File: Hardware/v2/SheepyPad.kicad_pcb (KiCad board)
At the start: 2 copper layers, 127.6 x 99.7 mm, 60 parts, among them SW1 SW_Push, SW2 Rotary_Encoder_Switch, U1 Sparkfun_Pro_Micro

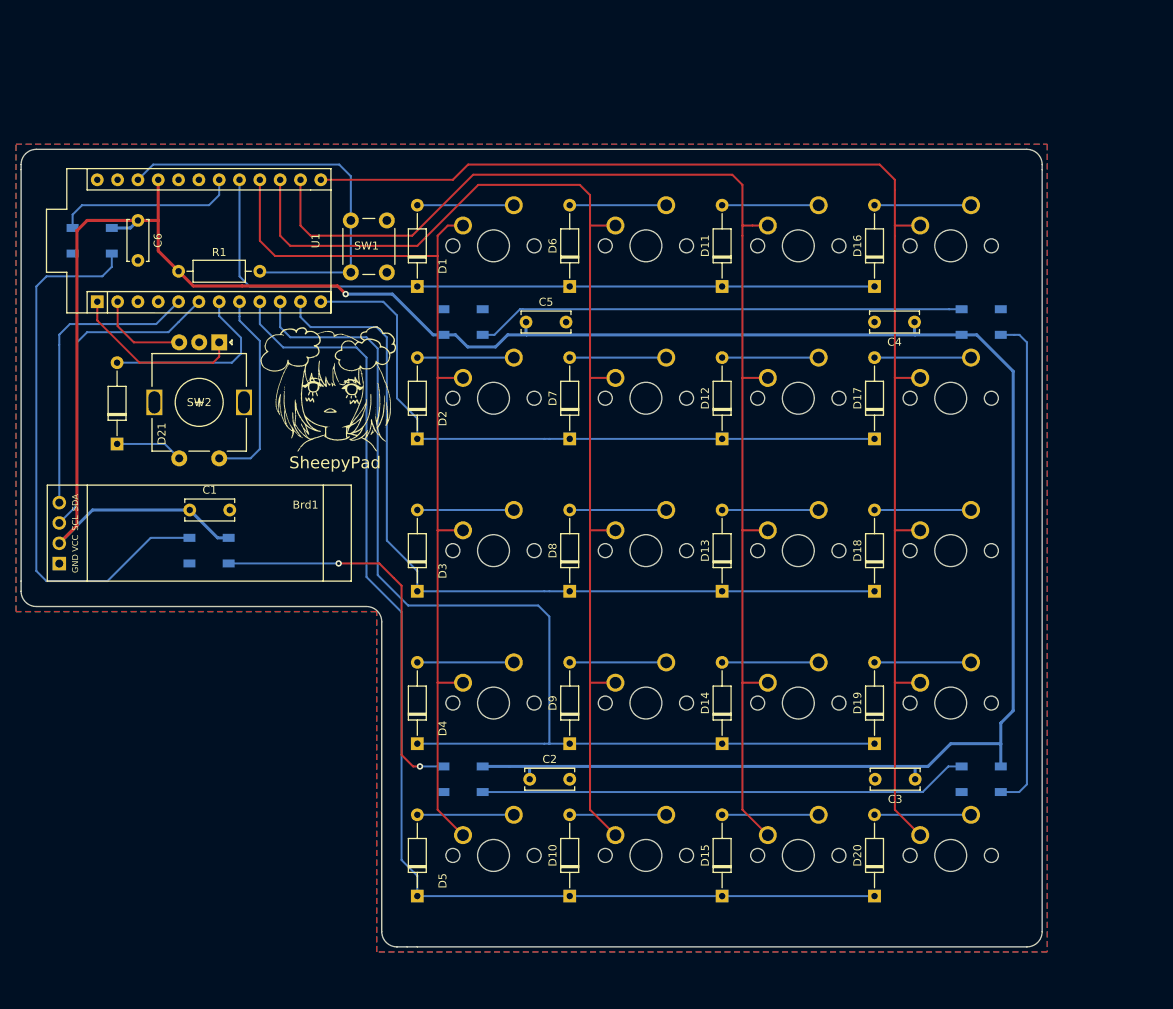
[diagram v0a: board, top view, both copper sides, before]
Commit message: Remove of redundant lib
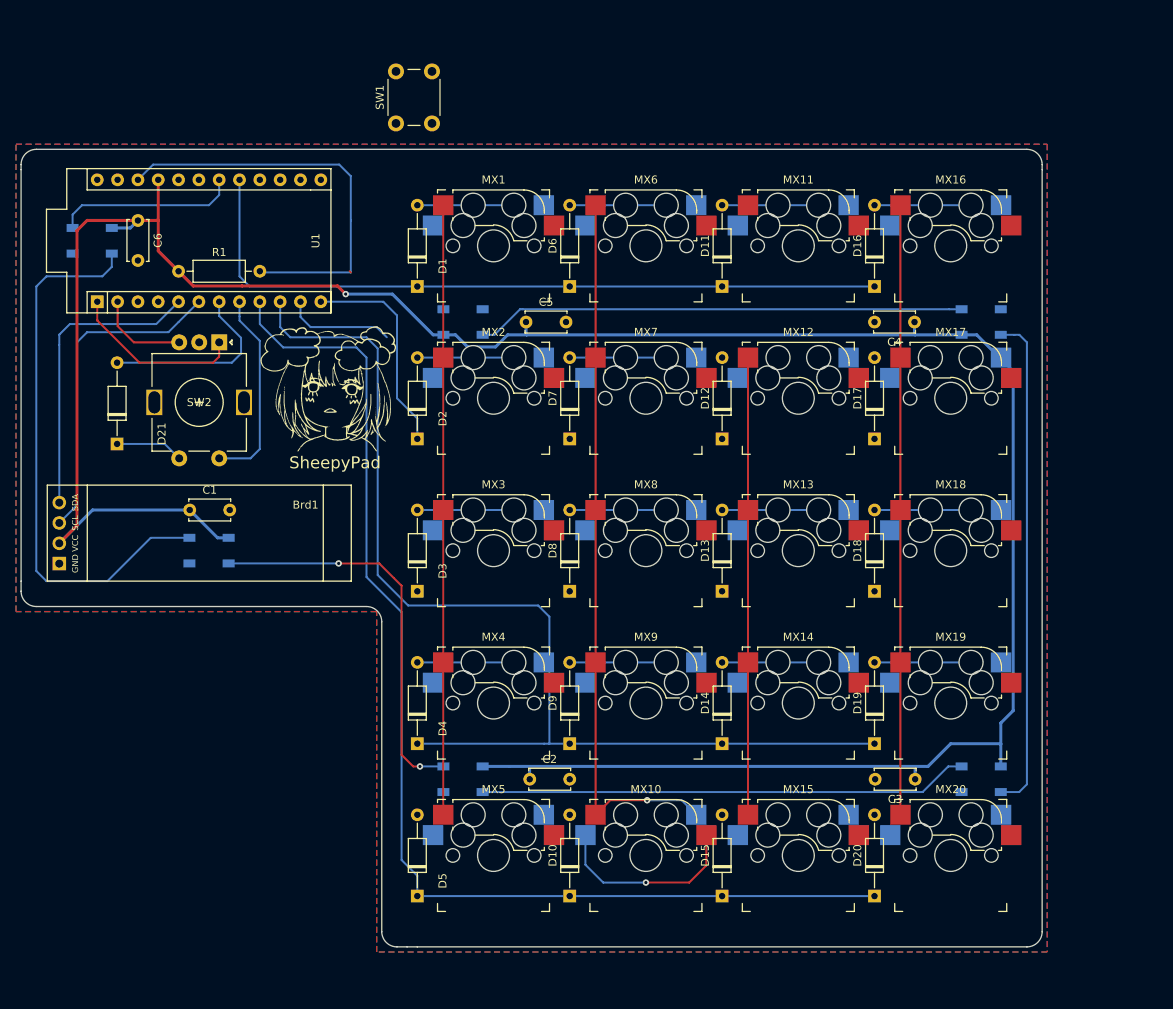
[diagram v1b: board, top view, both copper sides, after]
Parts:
- C1, C2, C3, C4, C5: footprint Capacitor_THT:C_Disc_D6.0mm_W2.5mm_P5.00mm -> Capacitor_THT:C_Disc_D5.0mm_W2.5mm_P5.00mm
- MX1, MX10, MX11, MX12, MX13, MX14, MX15, MX16, MX17, MX18, MX19, MX2, MX20, MX3, MX4, MX5, MX6, MX7, MX8, MX9: footprint MX_Only:MXOnly-1U-NoLED -> Keyswitches:Kailh_socket_MX_optional_reversible_FLIP
- moved SW1 12.2 mm to (104.0, 39.9), turned to 90 degrees
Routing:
- net /COL_3: track 160.5 -> 57.1 mm
- net /COL_4: track 169.3 -> 76.2 mm
- net /ROW_3: track 104.2 -> 13.8 mm
- net /ROW_2: track 83.9 -> 26.7 mm
- net /COL_2: track 144.0 -> 90.3 mm, vias 0 -> 1
- net /COL_1: track 120.1 -> 76.2 mm
- net Net-(D10-Pad2): track 12.1 -> 26.2 mm, vias 0 -> 1
- net Net-(D5-Pad2): track 12.1 -> 0.00 mm
- net Net-(D20-Pad2): track 12.1 -> 0.00 mm
- net Net-(D17-Pad2): track 12.1 -> 0.00 mm
- net Net-(D15-Pad2): track 12.1 -> 0.00 mm
- net Net-(D12-Pad2): track 12.1 -> 0.00 mm

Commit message: WIP v2
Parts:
- added D22: WS2812B, LED_SMD:LED_WS2812B_PLCC4_5.0x5.0mm_P3.2mm, F.Cu at (66.0, 54.6)
- added D23: WS2812B, LED_SMD:LED_WS2812B_PLCC4_5.0x5.0mm_P3.2mm, F.Cu at (180.3, 120.7)
- added D24: WS2812B, LED_SMD:LED_WS2812B_PLCC4_5.0x5.0mm_P3.2mm, F.Cu at (80.6, 93.3)
- added D25: WS2812B, LED_SMD:LED_WS2812B_PLCC4_5.0x5.0mm_P3.2mm, F.Cu at (180.3, 63.4)
- added D26: WS2812B, LED_SMD:LED_WS2812B_PLCC4_5.0x5.0mm_P3.2mm, F.Cu at (109.3, 120.7)
- added D27: WS2812B, LED_SMD:LED_WS2812B_PLCC4_5.0x5.0mm_P3.2mm, F.Cu at (109.3, 63.4)
- D1, D10, D11, D12, D13, D14, D15, D16, D17, D18, D19, D2, D20, D21, D3, D4, D5, D6, D7, D8, D9: footprint Diode_THT:D_DO-35_SOD27_P10.16mm_Horizontal -> Random-keyboard-parts:Diode_SMD_THT_DUAL
- moved C2 32.2 mm to (100.8, 147.3)
- moved C5 26.3 mm to (115.1, 38.9)
- moved C4 24.0 mm to (192.8, 62.7)
- moved C3 23.7 mm to (192.6, 122.3)
- moved D11 9.54 mm to (154.3, 59.8), turned to 270 degrees
- moved D12 9.54 mm to (154.3, 78.9), turned to 270 degrees
- moved D15 9.54 mm to (154.3, 136.0), turned to 270 degrees
- moved D13 9.54 mm to (154.3, 97.9), turned to 270 degrees
- moved D14 9.54 mm to (154.3, 117.0), turned to 270 degrees
- moved D1 9.54 mm to (116.2, 59.8), turned to 270 degrees
- moved D10 9.54 mm to (135.3, 136.0), turned to 270 degrees
- moved D2 9.54 mm to (116.2, 78.9), turned to 270 degrees
- moved D5 9.54 mm to (116.2, 136.0), turned to 270 degrees
- moved D6 9.54 mm to (135.3, 59.8), turned to 270 degrees
- moved D7 9.54 mm to (135.3, 78.9), turned to 270 degrees
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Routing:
- net +5V: track 324.3 -> 119.1 mm
- net /COL_3: track 57.1 -> 147.8 mm, vias 0 -> 5
- net /ROW_3: track 13.8 -> 100.3 mm
- net /COL_4: track 76.2 -> 147.8 mm, vias 0 -> 5
- net /COL_1: track 76.2 -> 147.8 mm, vias 0 -> 5
- net /ROW_2: track 26.7 -> 94.4 mm
- net Net-(D23-Pad2): track 62.6 -> 0.00 mm
- net Net-(D25-Pad2): track 61.2 -> 0.00 mm
- net Net-(D23-Pad4): track 61.2 -> 0.00 mm
- net /COL_2: track 90.3 -> 147.8 mm, vias 1 -> 5
- net Net-(D17-Pad2): track 0.00 -> 33.5 mm, vias 0 -> 1
- net Net-(D20-Pad2): track 0.00 -> 33.5 mm, vias 0 -> 1
- net Net-(D5-Pad2): track 0.00 -> 33.5 mm, vias 0 -> 1
- net Net-(D15-Pad2): track 0.00 -> 33.5 mm, vias 0 -> 1
- net Net-(D12-Pad2): track 0.00 -> 32.7 mm, vias 0 -> 1
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
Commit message: Update v2
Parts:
- removed the G*** at (93.3, 76.8)
- removed R1: 10K, Resistor_THT:R_Axial_DIN0207_L6.3mm_D2.5mm_P10.16mm_Horizontal
- added G***: LOGO, Logos:IronMan_small, B.Cu at (68.6, 96.2)
- added G***: LOGO, Logos:IronMan_small, F.Cu at (68.6, 96.2)
- added G***: LOGO, Logos:Sleepy, B.Cu at (97.1, 72.3)
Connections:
- D1 pad 1: /ROW_1 -> /ROW_0
- D10 pad 1: /ROW_5 -> /ROW_4
- D11 pad 1: /ROW_1 -> /ROW_0
- D12 pad 1: /ROW_2 -> /ROW_1
- D13 pad 1: /ROW_3 -> /ROW_2
- D14 pad 1: /ROW_4 -> /ROW_3
- D15 pad 1: /ROW_5 -> /ROW_4
- D16 pad 1: /ROW_1 -> /ROW_0
- D17 pad 1: /ROW_2 -> /ROW_1
- D18 pad 1: /ROW_3 -> /ROW_2
- D19 pad 1: /ROW_4 -> /ROW_3
- D2 pad 1: /ROW_2 -> /ROW_1
- D20 pad 1: /ROW_5 -> /ROW_4
- D21 pad 2: /COL_ENC_1 -> /COL_0
- D22 pad 1: (no net) -> +5V
- D22 pad 2: (no net) -> Net-(D22-Pad2)
- D22 pad 3: (no net) -> GND
- D22 pad 4: (no net) -> /GLOW_LED
- D23 pad 1: (no net) -> +5V
- D23 pad 2: (no net) -> Net-(D23-Pad2)
- D23 pad 3: (no net) -> GND
- D23 pad 4: (no net) -> Net-(D23-Pad4)
- D24 pad 1: (no net) -> +5V
- D24 pad 2: (no net) -> Net-(D24-Pad2)
- D24 pad 3: (no net) -> GND
- D24 pad 4: (no net) -> Net-(D22-Pad2)
- D25 pad 1: (no net) -> +5V
- D25 pad 2: (no net) -> Net-(D25-Pad2)
- D25 pad 3: (no net) -> GND
- D25 pad 4: (no net) -> Net-(D23-Pad2)
- D26 pad 1: (no net) -> +5V
- D26 pad 2: (no net) -> Net-(D23-Pad4)
- D26 pad 3: (no net) -> GND
- D26 pad 4: (no net) -> Net-(D24-Pad2)
- D27 pad 1: (no net) -> +5V
- D27 pad 2: (no net) -> Net-(D27-Pad2)
- D27 pad 3: (no net) -> GND
- D27 pad 4: (no net) -> Net-(D25-Pad2)
- D3 pad 1: /ROW_3 -> /ROW_2
- D4 pad 1: /ROW_4 -> /ROW_3
- D5 pad 1: /ROW_5 -> /ROW_4
- D6 pad 1: /ROW_1 -> /ROW_0
- D7 pad 1: /ROW_2 -> /ROW_1
- D8 pad 1: /ROW_3 -> /ROW_2
- D9 pad 1: /ROW_4 -> /ROW_3
- SW2 pad S2: /ROW_ENC_1 -> /ROW_0
- U1 pad 1: /ENC_A -> Net-(U1-Pad1)
- U1 pad 10: /ROW_4 -> /ROW_2
- U1 pad 11: /ROW_3 -> /ROW_1
- U1 pad 12: /ROW_2 -> /ROW_0
- U1 pad 13: /COL_4 -> /COL_0
- U1 pad 14: /COL_3 -> /COL_1
- U1 pad 16: /COL_1 -> /COL_3
- U1 pad 17: /ROW_1 -> /COL_4
- U1 pad 18: /GLOW_LED -> Net-(U1-Pad18)
- U1 pad 19: Net-(U1-Pad19) -> /ENC_A
- U1 pad 2: /ENC_B -> /DATA
- U1 pad 20: Net-(U1-Pad20) -> /ENC_B
- U1 pad 7: /COL_ENC_1 -> /GLOW_LED
- U1 pad 8: /ROW_ENC_1 -> /ROW_4
- U1 pad 9: /ROW_5 -> /ROW_3
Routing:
- net /ROW_5: track 129.6 -> 0.00 mm
- net +5V: track 119.1 -> 24.5 mm, vias 1 -> 0
- net /ROW_0: track 0.00 -> 85.6 mm
- net /RESET: track 51.7 -> 0.00 mm
- net Net-(D22-Pad2): track 69.6 -> 21.9 mm
- net /ROW_4: track 129.0 -> 84.3 mm
- net /SCL: track 40.8 -> 3.13 mm
- net /SDA: track 37.6 -> 0.00 mm
- net /ROW_ENC_1: track 25.0 -> 0.00 mm
- net /COL_ENC_1: track 23.5 -> 0.00 mm
- net /GLOW_LED: track 22.9 -> 0.00 mm
- net /ENC_A: track 22.5 -> 0.64 mm
- net Net-(D24-Pad2): track 21.4 -> 0.00 mm, vias 1 -> 0
- net /ROW_3: track 100.3 -> 84.2 mm
- net /ROW_1: track 99.5 -> 86.6 mm
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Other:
- board text added: "SheepyPad v2"
- board text removed: "SheepyPad"

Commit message: WIP
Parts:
- added REF**: PJ-3200B-4A, Random-keyboard-parts:PJ-3200B-4A, B.Cu at (98.9, 43.3)
- added REF**: PJ-3200B-4A, Random-keyboard-parts:PJ-3200B-4A, F.Cu at (101.2, 43.3)
- U1: footprint Arduino:Sparkfun_Pro_Micro -> Arduino:Sparkfun_Pro_Micro_reversible
- moved U1 17.1 mm to (79.5, 55.0)
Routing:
- net +5V: track 24.5 -> 0.00 mm
- net Net-(D22-Pad2): track 21.9 -> 0.00 mm
- net /SCL: track 3.13 -> 0.00 mm
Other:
- board text added: "Pro Micro's back side up"

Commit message: WIP v2
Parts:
- removed REF** (x2): PJ-3200B-4A, Random-keyboard-parts:PJ-3200B-4A
- added J1: AudioJack4, Random-keyboard-parts:PJ-3200B-4A, B.Cu at (99.9, 43.2)
- added J1: AudioJack4, Random-keyboard-parts:PJ-3200B-4A, F.Cu at (102.2, 43.2)
- added JP1: Serial/SCL Jumper, Jumper:SolderJumper-3_P1.3mm_Open_Pad1.0x1.5mm, F.Cu at (76.4, 29.3)
- added JP2: SDA Jumper, Jumper:SolderJumper-2_P1.3mm_Open_Pad1.0x1.5mm, F.Cu at (84.9, 37.4)
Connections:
- net +5V renamed VCC

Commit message: WIP v2
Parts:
- moved C3 50.6 mm to (198.4, 72.1)
- moved C4 4.58 mm to (197.4, 62.9)
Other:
- board size 127.6 x 99.7 mm -> 130.2 x 99.7 mm

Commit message: WIP v2
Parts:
- added JP1: Serial/SCL Jumper, Jumper:SolderJumper-3_P1.3mm_Open_Pad1.0x1.5mm, B.Cu at (93.8, 53.7)
- added JP2: SDA Jumper, Jumper:SolderJumper-2_P1.3mm_Open_Pad1.0x1.5mm, B.Cu at (93.8, 50.1)
- added REF**: Jack_3.5mm_PJ320D_Horizontal, Connector_Audio:Jack_3.5mm_PJ320D_Horizontal, F.Cu at (118.9, 39.9)
- moved C3 54.0 mm to (175.1, 120.7)
- moved C2 30.1 mm to (114.9, 120.7)
- moved JP1 29.9 mm to (93.8, 53.7), turned to 90 degrees
- moved C5 24.2 mm to (114.3, 63.1)
- moved C4 22.0 mm to (175.4, 63.4)
- moved JP2 15.5 mm to (93.8, 50.1), turned to 270 degrees
- moved C1 9.41 mm to (86.2, 93.3)
- moved D21 5.02 mm to (68.1, 75.1), turned to 0 degrees
- moved C6 3.02 mm to (70.1, 54.6), turned to 0 degrees
- moved D22 1.26 mm to (64.8, 54.6) (x2)
- moved SW2 1.26 mm to (80.7, 67.3)
- moved U1 1.26 mm to (78.2, 55.0)
- moved D27 0.81 mm to (108.6, 63.1), turned to 180 degrees (x2)
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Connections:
- U1 pad 19: /ENC_A -> /ENC_B
- U1 pad 20: /ENC_B -> /ENC_A
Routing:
- net VCC: track 0.00 -> 213.6 mm
- net Net-(D23-Pad4): track 0.00 -> 81.6 mm, vias 0 -> 3
- net Net-(D25-Pad2): track 0.00 -> 78.9 mm, vias 0 -> 4
- net /ROW_4: track 84.3 -> 151.7 mm
- net Net-(D23-Pad2): track 0.00 -> 63.7 mm, vias 0 -> 2
- net Net-(D24-Pad2): track 0.00 -> 51.4 mm, vias 0 -> 2
- net /SCL: track 0.00 -> 26.7 mm, vias 0 -> 1
- net /ROW_3: track 84.2 -> 103.5 mm
- net /SDA: track 0.00 -> 18.8 mm, vias 0 -> 1
- net /DATA: track 0.00 -> 12.6 mm
- net /ROW_2: track 86.6 -> 98.2 mm
- net /ENC_B: track 0.00 -> 9.29 mm
- net Net-(D21-Pad1): track 4.37 -> 13.1 mm
- net /ENC_A: track 0.64 -> 7.22 mm
- net Net-(D22-Pad2): track 0.00 -> 6.40 mm, vias 0 -> 2
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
